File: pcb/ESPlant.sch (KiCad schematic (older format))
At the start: 23 parts, among them J1 Power, J2 TAG, J3 PUMP, J4 Soil Moisture, Q1 Q_NPN_BCE, Q2 Pump Driver, U1 ESP32-WROOM-32, U2 Si7021-A20, U3 LD1117S33TR_SOT223

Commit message: Official revision 0.1!  Adding revision info and logo to PCB
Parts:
- added C?: 10uF, Capacitor_SMD:C_0603_1608Metric_Pad1.05x0.95mm_HandSolder, symbol Device:C
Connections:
- net +BATT: now also C?.1
- net GNDREF: now also C?.2
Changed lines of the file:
@@
 Wire Wire Line
 	3500 3650 3650 3650
+$Comp
+L Device:C C?
+U 1 1 5E648717
+P 10000 3400
+F 0 "C?" H 10115 3446 50  0000 L CNN
+F 1 "10uF" H 10115 3355 50  0000 L CNN
+F 2 "Capacitor_SMD:C_0603_1608Metric_Pad1.05x0.95mm_HandSolder" H 10038 3250 50  0001 C CNN
+F 3 "~" H 10000 3400 50  0001 C CNN
+	1    10000 3400
+	0    -1   -1   0
+$EndComp
+$Comp
+L power:GNDREF #PWR?
+U 1 1 5E65A37A
+P 10250 3400
+F 0 "#PWR?" H 10250 3150 50  0001 C CNN
+F 1 "GNDREF" V 10255 3272 50  0000 R CNN
+F 2 "" H 10250 3400 50  0001 C CNN
+F 3 "" H 10250 3400 50  0001 C CNN
+	1    10250 3400
+	0    -1   -1   0
+$EndComp
+Wire Wire Line
+	10150 3400 10250 3400
+Wire Wire Line
+	9850 3400 9700 3400
+Connection ~ 9700 3400
 $EndSCHEMATC

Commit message: PCB Revision 0.2 fixing Q1 footprint from NPN BCE to BEC to match more common parts. Minor routing revisions
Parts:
- removed Q1: Q_NPN_BCE, Package_TO_SOT_SMD:SOT-23_Handsoldering, symbol Device:Q_NPN_BCE
- added Q1: MMBT2222ALT1G, Package_TO_SOT_SMD:SOT-23_Handsoldering, symbol Device:Q_NPN_BEC
- gave numbers to parts that had none: 1
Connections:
- net GNDREF: now also Q1.2 (E)
- net at U2.2 (GND): now also Q1.3 (C)
- net at R2.1: now also Q1.1 (B)
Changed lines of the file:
@@
 Wire Wire Line
 	9700 3750 9900 3750
-$Comp
-L Diode:LL4148 D1
-U 1 1 5E61A832
-P 6900 4950
-F 0 "D1" H 6900 5166 50  0000 C CNN
-F 1 "LL4148" H 6900 5075 50  0000 C CNN
-F 2 "Diode_SMD:D_MiniMELF" H 6900 4775 50  0001 C CNN
-F 3 "http://www.vishay.com/docs/85557/ll4148.pdf" H 6900 4950 50  0001 C CNN
-	1    6900 4950
-	0    1    1    0
-$EndComp
 Text GLabel 3650 3850 2    50   Input ~ 0
 PUMP_EN
@@
 F 3 "" H 2850 6800 50  0001 C CNN
 	1    2850 6800
-	1    0    0    -1
-$EndComp
-$Comp
-L Device:Q_NPN_BCE Q1
-U 1 1 5E5D3D4B
-P 2750 6500
-F 0 "Q1" H 2940 6500 50  0000 L CNN
-F 1 "Q_NPN_BCE" H 2941 6455 50  0001 L CNN
-F 2 "Package_TO_SOT_SMD:SOT-23_Handsoldering" H 2950 6600 50  0001 C CNN
-F 3 "~" H 2750 6500 50  0001 C CNN
-	1    2750 6500
 	1    0    0    -1
 $EndComp
@@
 	3500 3650 3650 3650
 $Comp
-L Device:C C?
+L Device:C C4
 U 1 1 5E648717
 P 10000 3400
-F 0 "C?" H 10115 3446 50  0000 L CNN
+F 0 "C4" H 10115 3446 50  0000 L CNN
 F 1 "10uF" H 10115 3355 50  0000 L CNN
 F 2 "Capacitor_SMD:C_0603_1608Metric_Pad1.05x0.95mm_HandSolder" H 10038 3250 50  0001 C CNN
@@
 $EndComp
 $Comp
-L power:GNDREF #PWR?
+L power:GNDREF #PWR0101
 U 1 1 5E65A37A
 P 10250 3400
-F 0 "#PWR?" H 10250 3150 50  0001 C CNN
+F 0 "#PWR0101" H 10250 3150 50  0001 C CNN
 F 1 "GNDREF" V 10255 3272 50  0000 R CNN
 F 2 "" H 10250 3400 50  0001 C CNN
@@
 	9850 3400 9700 3400
 Connection ~ 9700 3400
+$Comp
+L Device:Q_NPN_BEC Q1
+U 1 1 5E6793F6
+P 2750 6500
+F 0 "Q1" H 2941 6546 50  0000 L CNN
+F 1 "MMBT2222ALT1G" H 2941 6455 50  0000 L CNN
+F 2 "Package_TO_SOT_SMD:SOT-23_Handsoldering" H 2940 6409 50  0001 L CNN
+F 3 "http://www.onsemi.com/pub/Collateral/MMBT2222LT1-D.PDF" H 2750 6500 50  0001 C CNN
+	1    2750 6500
+	1    0    0    -1
+$EndComp
+$Comp
+L Diode:LL4148 D1
+U 1 1 5E61A832
+P 6900 4950
+F 0 "D1" H 6900 5166 50  0000 C CNN
+F 1 "LL4148" H 6900 5075 50  0000 C CNN
+F 2 "Diode_SMD:D_MiniMELF" H 6900 4775 50  0001 C CNN
+F 3 "http://www.vishay.com/docs/85557/ll4148.pdf" H 6900 4950 50  0001 C CNN
+	1    6900 4950
+	0    1    1    0
+$EndComp
 $EndSCHEMATC

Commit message: Initial ESPlant Arduino based software.  Updated battery voltage divider values in schematic.
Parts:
- R3: value R -> 33k
- R4: value R -> 51k
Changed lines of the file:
@@
 P 5900 2000
 F 0 "R4" H 5970 2046 50  0000 L CNN
-F 1 "R" H 5970 1955 50  0000 L CNN
+F 1 "51k" H 5970 1955 50  0000 L CNN
 F 2 "Resistor_SMD:R_0603_1608Metric_Pad1.05x0.95mm_HandSolder" V 5830 2000 50  0001 C CNN
 F 3 "~" H 5900 2000 50  0001 C CNN
@@
 P 5900 1600
 F 0 "R3" H 5970 1646 50  0000 L CNN
-F 1 "R" H 5970 1555 50  0000 L CNN
+F 1 "33k" H 5970 1555 50  0000 L CNN
 F 2 "Resistor_SMD:R_0603_1608Metric_Pad1.05x0.95mm_HandSolder" V 5830 1600 50  0001 C CNN
 F 3 "~" H 5900 1600 50  0001 C CNN

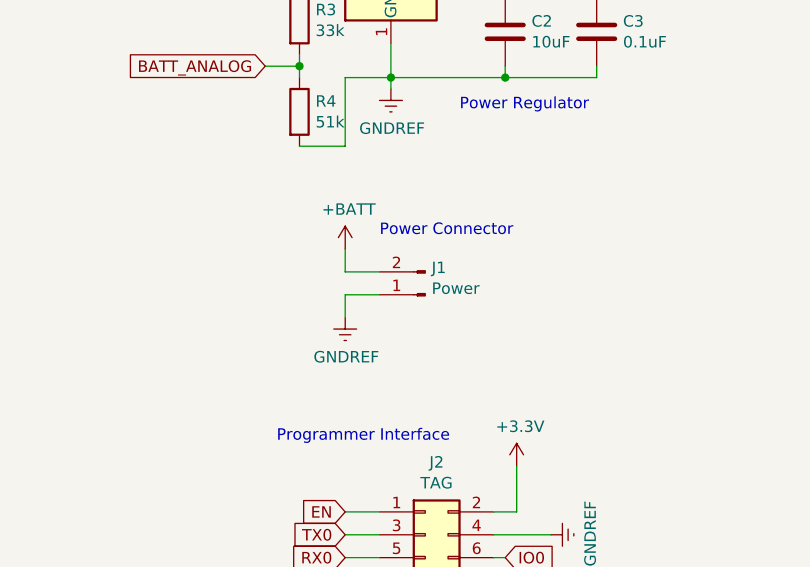
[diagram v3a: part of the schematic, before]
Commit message: Flipping batter positive and negative pins and added '+' symbol to resolve ambiguity during assembly
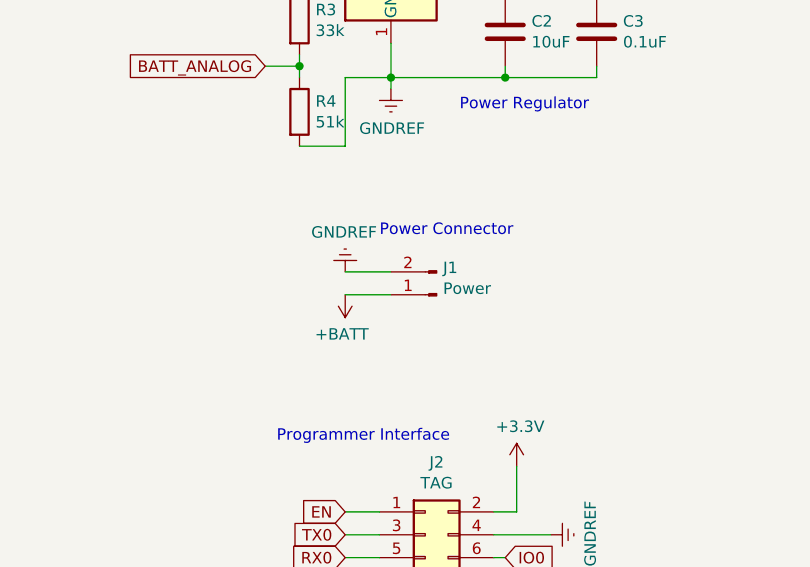
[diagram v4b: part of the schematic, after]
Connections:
- net +BATT: now also J1.1 (Pin_1); no longer J1.2 (Pin_2)
- net GNDREF: now also J1.2 (Pin_2); no longer J1.1 (Pin_1)
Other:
- moved on the sheet: J1
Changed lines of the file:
@@
 	3650 3750 3500 3750
-$Comp
-L Connector:Conn_01x02_Male J1
-U 1 1 5E5C5FA9
-P 6450 2800
-F 0 "J1" H 6422 2682 50  0000 R CNN
-F 1 "Power" H 6422 2773 50  0000 R CNN
-F 2 "Connector_PinHeader_2.54mm:PinHeader_1x02_P2.54mm_Vertical" H 6450 2800 50  0001 C CNN
-F 3 "~" H 6450 2800 50  0001 C CNN
-	1    6450 2800
-	-1   0    0    1
-$EndComp
 $Comp
 L power:+BATT #PWR08
 U 1 1 5E5C755D
-P 6100 2600
-F 0 "#PWR08" H 6100 2450 50  0001 C CNN
-F 1 "+BATT" H 6115 2773 50  0000 C CNN
-F 2 "" H 6100 2600 50  0001 C CNN
-F 3 "" H 6100 2600 50  0001 C CNN
-	1    6100 2600
-	1    0    0    -1
-$EndComp
-Wire Wire Line
-	6100 2700 6250 2700
-Wire Wire Line
-	6100 2600 6100 2700
+P 6100 2800
+F 0 "#PWR08" H 6100 2650 50  0001 C CNN
+F 1 "+BATT" H 6115 2973 50  0000 C CNN
+F 2 "" H 6100 2800 50  0001 C CNN
+F 3 "" H 6100 2800 50  0001 C CNN
+	1    6100 2800
+	-1   0    0    1
+$EndComp
 $Comp
 L power:GNDREF #PWR09
 U 1 1 5E5CAF58
-P 6100 2900
-F 0 "#PWR09" H 6100 2650 50  0001 C CNN
-F 1 "GNDREF" H 6105 2727 50  0000 C CNN
-F 2 "" H 6100 2900 50  0001 C CNN
-F 3 "" H 6100 2900 50  0001 C CNN
-	1    6100 2900
-	1    0    0    -1
-$EndComp
-Wire Wire Line
-	6250 2800 6100 2800
-Wire Wire Line
-	6100 2800 6100 2900
+P 6100 2700
+F 0 "#PWR09" H 6100 2450 50  0001 C CNN
+F 1 "GNDREF" H 6105 2527 50  0000 C CNN
+F 2 "" H 6100 2700 50  0001 C CNN
+F 3 "" H 6100 2700 50  0001 C CNN
+	1    6100 2700
+	-1   0    0    1
+$EndComp
 Wire Wire Line
 	6750 3750 6850 3750
@@
 	0    1    1    0
 $EndComp
+$Comp
+L Connector:Conn_01x02_Male J1
+U 1 1 5E5C5FA9
+P 6500 2800
+F 0 "J1" H 6472 2682 50  0000 R CNN
+F 1 "Power" H 6472 2773 50  0000 R CNN
+F 2 "Connector_PinHeader_2.54mm:PinHeader_1x02_P2.54mm_Vertical" H 6500 2800 50  0001 C CNN
+F 3 "~" H 6500 2800 50  0001 C CNN
+	1    6500 2800
+	-1   0    0    1
+$EndComp
+Wire Wire Line
+	6100 2800 6300 2800
+Wire Wire Line
+	6100 2700 6300 2700
 $EndSCHEMATC
